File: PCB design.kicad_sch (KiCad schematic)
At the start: 19 parts

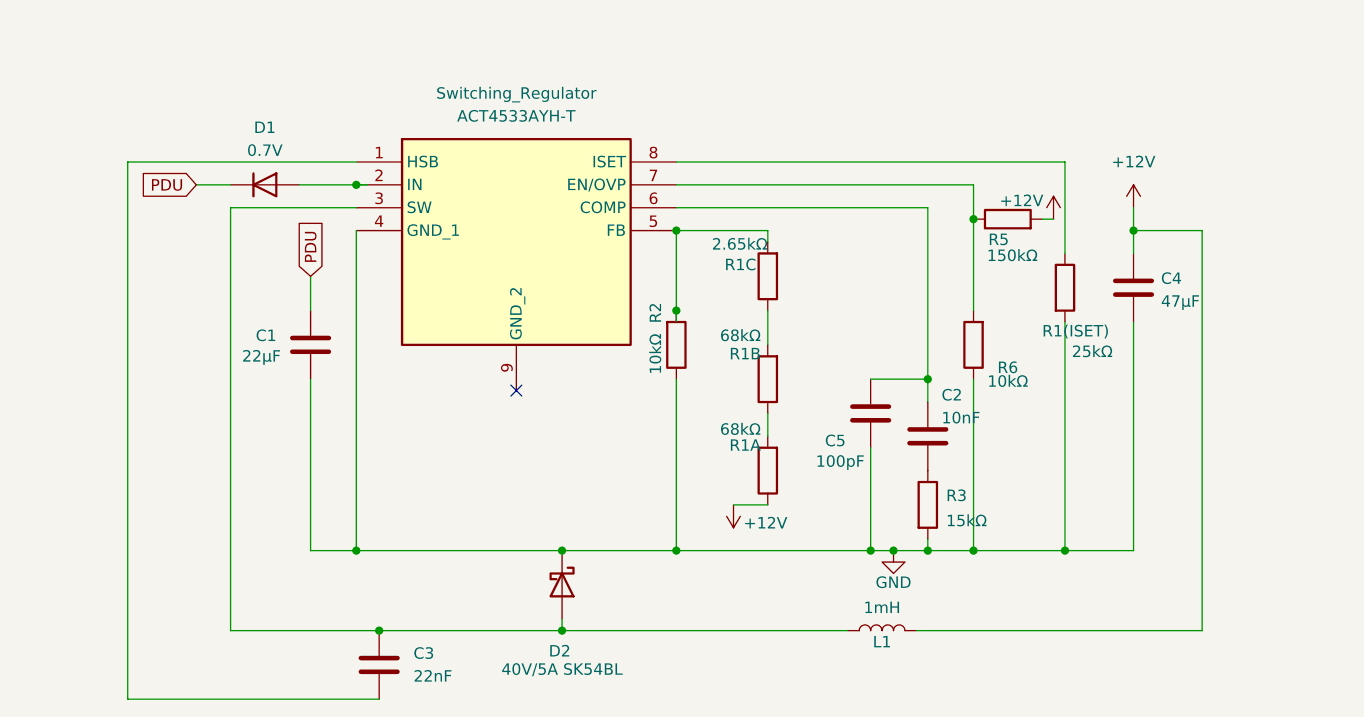
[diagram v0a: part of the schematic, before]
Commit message: added footprints to the components we have to buy.
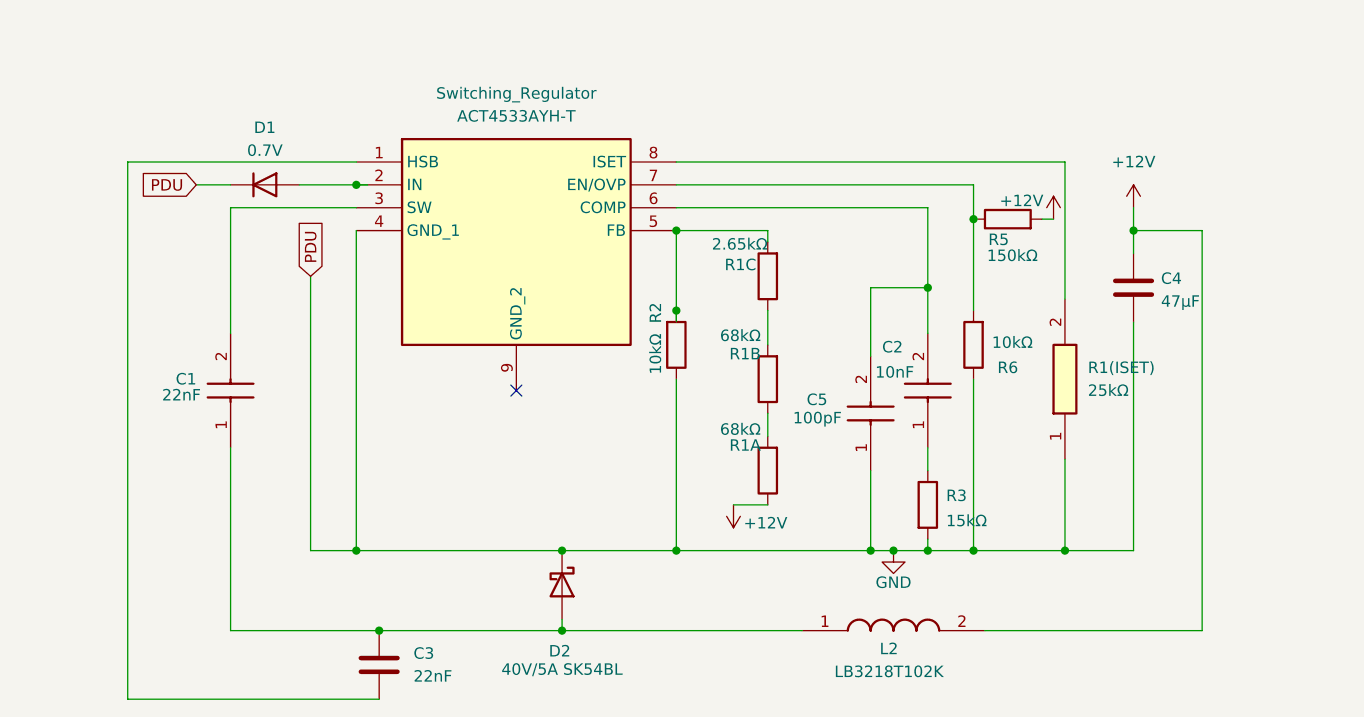
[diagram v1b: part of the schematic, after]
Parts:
- removed C1: 22µF, symbol Device:C
- removed C2: 10nF, symbol Device:C
- removed C5: 100pF, symbol Device:C
- removed L1: 1mH, symbol Device:L
- removed R1(ISET): 25kΩ, symbol Device:R
- added C1: 22nF, CAPPA3500W66L1100D600, symbol MKP1839110631:MKP1839110631
- added C2: 10nF, D103K69Y5PL63L0R, symbol D103K69Y5PL63L0R:D103K69Y5PL63L0R
- added C5: 100pF, CAPPA3100W60L1100D500, symbol MKT1813322405G:MKT1813322405G
- added L2: LB3218T102K, INDC3218X200N, symbol LB3218T102K:LB3218T102K
- added R1(ISET): 25kΩ, RESAD1526W69L610D229, symbol RN55E2502BRE6:RN55E2502BRE6
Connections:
- net PDU is gone; now on net GND: D1.1 (K), Male_Connector.2
- net +12V: now also L2.2
- net GND: now also C5.1 (+), R1(ISET).1
- net at C3.1, D2.2 (A): now also C1.1 (+), L2.1; no longer Switching_Regulator.3 (SW)
- net at Switching_Regulator.6 (COMP): now also C2.2, C5.2 (-)
- net at R3.1: now also C2.1
- net at Switching_Regulator.8 (ISET): now also R1(ISET).2
- new net: C1.2 (-), Switching_Regulator.3 (SW)

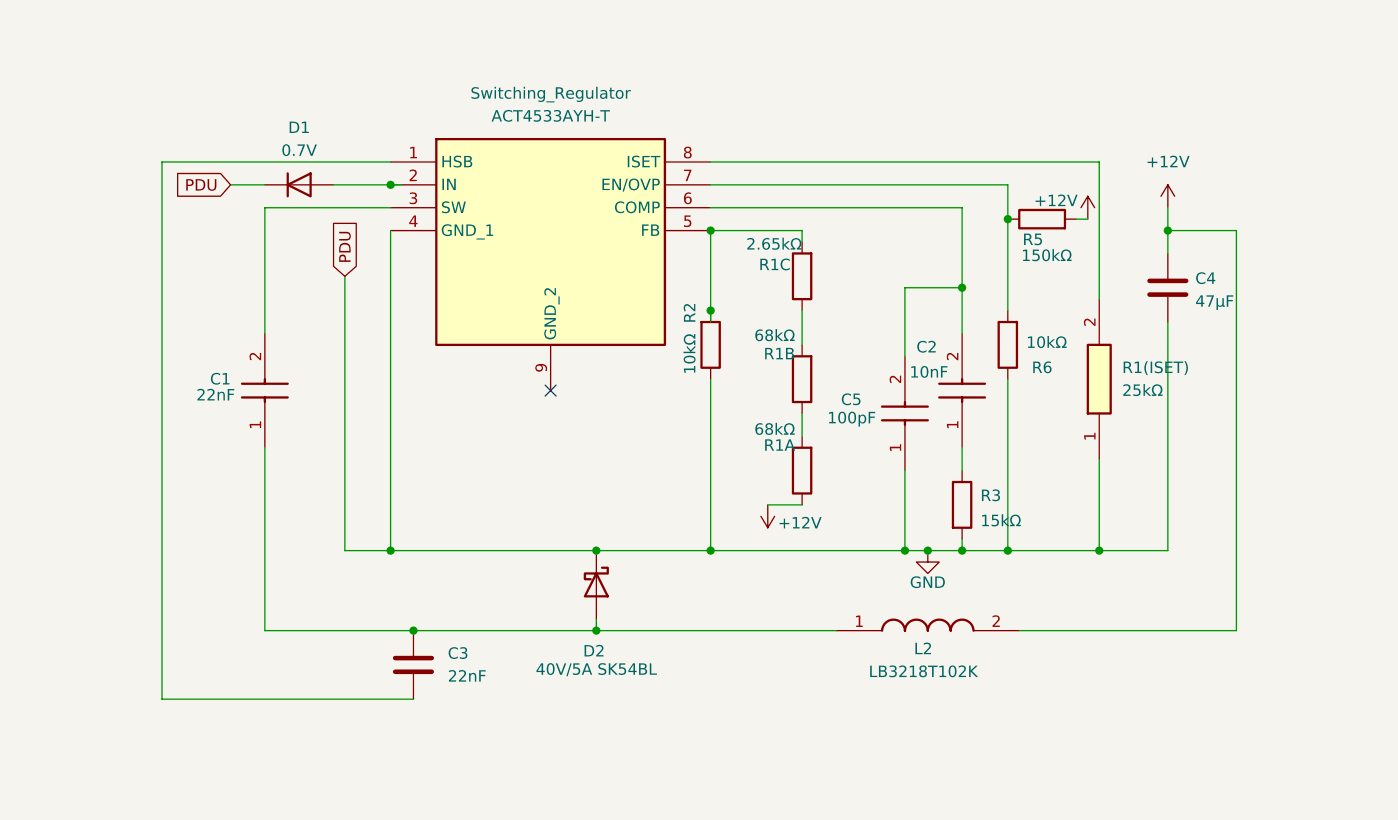
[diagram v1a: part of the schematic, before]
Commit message: added schotsky diode.
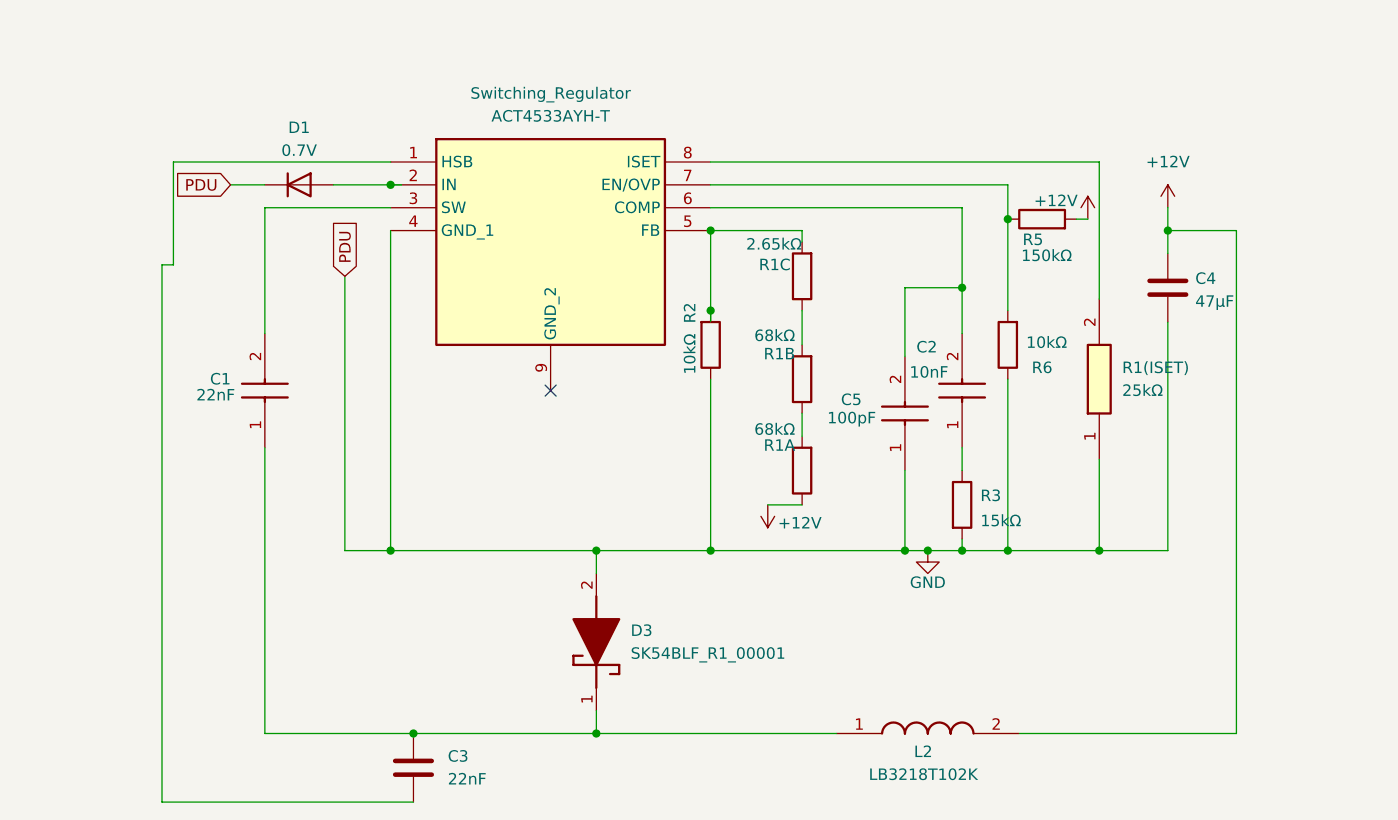
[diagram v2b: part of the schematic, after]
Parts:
- removed D2: 40V/5A SK54BL, Diode_SMD:D_0603_1608Metric, symbol Device:D_Schottky
- added D3: SK54BLF_R1_00001, SODFL5336X110N, symbol SK54BLF_R1_00001:SK54BLF_R1_00001
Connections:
- net GND: now also D3.2 (A)
- net at C1.1 (+), C3.1, L2.1: now also D3.1 (K)
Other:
- moved on the sheet: C3, L2

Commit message: Added a SMD footprint to all components, excluding the connectors
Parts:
- 150k1: renamed from 150kΩ; footprint (none) -> Resistor_SMD:R_01005_0402Metric_Pad0.57x0.30mm_HandSolder
- C1: footprint CAPPA3500W66L1100D600 -> Capacitor_SMD:C_01005_0402Metric_Pad0.57x0.30mm_HandSolder
- C2: footprint D103K69Y5PL63L0R -> Capacitor_SMD:C_01005_0402Metric_Pad0.57x0.30mm_HandSolder
- C3: footprint (none) -> Capacitor_SMD:C_1206_3216Metric_Pad1.33x1.80mm_HandSolder
- C4: footprint (none) -> Capacitor_SMD:C_1808_4520Metric_Pad1.72x2.30mm_HandSolder
- C5: footprint CAPPA3100W60L1100D500 -> Capacitor_SMD:C_1808_4520Metric_Pad1.72x2.30mm_HandSolder
- D1: footprint (none) -> Diode_SMD:D_2010_5025Metric_Pad1.52x2.65mm_HandSolder
- D3: footprint SODFL5336X110N -> Diode_SMD:D_2010_5025Metric_Pad1.52x2.65mm_HandSolder
- Female_Connector1: renamed from Female_Connector; footprint SFM-105-YY-XXX-D-A-K-TR -> Footprints:RESAD1526W69L610D229
- L2: footprint INDC3218X200N -> Inductor_SMD:L_10.4x10.4_H4.8
- Male_Connector1: renamed from Male_Connector; footprint TFM-105-02-XXX-D-WT -> Footprints:TFM-105-02-XXX-D-WT
- R1(ISET)1: renamed from R1(ISET); footprint RESAD1526W69L610D229 -> Resistor_SMD:R_01005_0402Metric_Pad0.57x0.30mm_HandSolder
- R1A1: renamed from R1A; footprint (none) -> Resistor_SMD:R_01005_0402Metric_Pad0.57x0.30mm_HandSolder
- R1B1: renamed from R1B; footprint (none) -> Resistor_SMD:R_01005_0402Metric_Pad0.57x0.30mm_HandSolder
- R1C1: renamed from R1C; footprint (none) -> Resistor_SMD:R_01005_0402Metric_Pad0.57x0.30mm_HandSolder
- R2, R3, R6: footprint (none) -> Resistor_SMD:R_01005_0402Metric_Pad0.57x0.30mm_HandSolder
- Switching_Regulator1: renamed from Switching_Regulator; footprint SOIC127P600X170-9N -> Footprints:SOIC127P600X170-9N
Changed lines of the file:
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@@
 	(wire
 		(pts
-			(xy 92.71 81.28) (xy 92.71 69.85)
+			(xy 91.44 69.85) (xy 91.44 140.97)
 		)
 		(stroke
@@
 	(wire
 		(pts
-			(xy 92.71 69.85) (xy 116.84 69.85)
+			(xy 91.44 69.85) (xy 116.84 69.85)
 		)
 		(stroke
@@
 	(wire
 		(pts
-			(xy 91.44 140.97) (xy 91.44 81.28)
-		)
-		(stroke
-			(width 0)
-			(type default)
-		)
-	)
-	(wire
-		(pts
 			(xy 152.4 69.85) (xy 195.58 69.85)
 		)
@@
 	(wire
 		(pts
-			(xy 91.44 81.28) (xy 92.71 81.28)
-		)
-		(stroke
-			(width 0)
-			(type default)
-		)
-	)
-	(wire
-		(pts
 			(xy 102.87 133.35) (xy 119.38 133.35)
 		)
@@
 		(in_pos_files yes)
 		(dnp no)
-		(property "Reference" "150kΩ"
+		(property "Reference" "150k1"
 			(at 189.738 80.264 90)
 			(show_name no)
@@
 			)
 		)
-		(property "Footprint" ""
+		(property "Footprint" "Resistor_SMD:R_01005_0402Metric_Pad0.57x0.30mm_HandSolder"
 			(at 189.23 77.978 90)
 			(hide yes)
@@
 			(project "PCB design"
 				(path "/1ee13f0d-22f2-4352-9e68-759581f4b836"
-					(reference "150kΩ")
+					(reference "150k1")
 					(unit 1)
 				)
@@
 			)
 		)
-		(property "Footprint" "INDC3218X200N"
+		(property "Footprint" "Inductor_SMD:L_10.4x10.4_H4.8"
 			(at 182.88 229.54 0)
 			(hide yes)
@@
 		(dnp no)
 		(fields_autoplaced yes)
-		(property "Reference" "R1(ISET)"
+		(property "Reference" "R1(ISET)1"
 			(at 198.12 92.7099 90)
 			(show_name no)
@@
 			)
 		)
-		(property "Footprint" "RESAD1526W69L610D229"
+		(property "Footprint" "Resistor_SMD:R_01005_0402Metric_Pad0.57x0.30mm_HandSolder"
 			(at 291.77 88.9 0)
 			(hide yes)
@@
 			(project "PCB design"
 				(path "/1ee13f0d-22f2-4352-9e68-759581f4b836"
-					(reference "R1(ISET)")
+					(reference "R1(ISET)1")
 					(unit 1)
 				)
@@
 			)
 		)
-		(property "Footprint" "SODFL5336X110N"
+		(property "Footprint" "Diode_SMD:D_2010_5025Metric_Pad1.52x2.65mm_HandSolder"
 			(at 233.35 120.65 0)
 			(hide yes)
@@
 			)
 		)
-		(property "Footprint" "CAPPA3500W66L1100D600"
+		(property "Footprint" "Capacitor_SMD:C_01005_0402Metric_Pad0.57x0.30mm_HandSolder"
 			(at 199.06 92.71 0)
 			(hide yes)
@@
 			)
 		)
-		(property "Footprint" ""
+		(property "Footprint" "Resistor_SMD:R_01005_0402Metric_Pad0.57x0.30mm_HandSolder"
 			(at 187.198 90.17 90)
 			(hide yes)
@@
 		(in_pos_files yes)
 		(dnp no)
-		(property "Reference" "R1A"
+		(property "Reference" "R1A1"
 			(at 161.798 101.346 0)
 			(show_name no)
@@
 			)
 		)
-		(property "Footprint" ""
+		(property "Footprint" "Resistor_SMD:R_01005_0402Metric_Pad0.57x0.30mm_HandSolder"
 			(at 164.338 104.14 90)
 			(hide yes)
@@
 			(project "PCB design"
 				(path "/1ee13f0d-22f2-4352-9e68-759581f4b836"
-					(reference "R1A")
+					(reference "R1A1")
 					(unit 1)
 				)
@@
 		(dnp no)
 		(fields_autoplaced yes)
-		(property "Reference" "Female_Connector"
+		(property "Reference" "Female_Connector1"
 			(at 259.08 83.82 0)
 			(show_name no)
@@
 			)
 		)
-		(property "Footprint" "SFM-105-YY-XXX-D-A-K-TR"
+		(property "Footprint" "Footprints:RESAD1526W69L610D229"
 			(at 266.7 186.36 0)
 			(hide yes)
@@
 			(project "PCB design"
 				(path "/1ee13f0d-22f2-4352-9e68-759581f4b836"
-					(reference "Female_Connector")
+					(reference "Female_Connector1")
 					(unit 1)
 				)
@@
 		(in_pos_files yes)
 		(dnp no)
-		(property "Reference" "R1C"
+		(property "Reference" "R1C1"
 			(at 161.29 81.28 0)
 			(show_name no)
@@
 			)
 		)
-		(property "Footprint" ""
+		(property "Footprint" "Resistor_SMD:R_01005_0402Metric_Pad0.57x0.30mm_HandSolder"
 			(at 164.338 82.55 90)
 			(hide yes)
@@
 			(project "PCB design"
 				(path "/1ee13f0d-22f2-4352-9e68-759581f4b836"
-					(reference "R1C")
+					(reference "R1C1")
 					(unit 1)
 				)
@@
 		(in_pos_files yes)
 		(dnp no)
-		(property "Reference" "R1B"
+		(property "Reference" "R1B1"
 			(at 161.798 91.186 0)
 			(show_name no)
@@
 			)
 		)
-		(property "Footprint" ""
+		(property "Footprint" "Resistor_SMD:R_01005_0402Metric_Pad0.57x0.30mm_HandSolder"
 			(at 164.338 93.98 90)
 			(hide yes)
@@
 			(project "PCB design"
 				(path "/1ee13f0d-22f2-4352-9e68-759581f4b836"
-					(reference "R1B")
+					(reference "R1B1")
 					(unit 1)
 				)
@@
 			)
 		)
-		(property "Footprint" ""
+		(property "Footprint" "Resistor_SMD:R_01005_0402Metric_Pad0.57x0.30mm_HandSolder"
 			(at 178.562 107.95 90)
 			(hide yes)
@@
 			)
 		)
-		(property "Footprint" ""
+		(property "Footprint" "Diode_SMD:D_2010_5025Metric_Pad1.52x2.65mm_HandSolder"
 			(at 106.68 72.39 0)
 			(hide yes)
@@
 			)
 		)
-		(property "Footprint" ""
+		(property "Footprint" "Capacitor_SMD:C_1808_4520Metric_Pad1.72x2.30mm_HandSolder"
 			(at 204.1652 87.63 0)
 			(hide yes)
@@
 		(dnp no)
 		(fields_autoplaced yes)
-		(property "Reference" "Male_Connector"
+		(property "Reference" "Male_Connector1"
 			(at 40.64 85.09 0)
 			(show_name no)
@@
 			)
 		)
-		(property "Footprint" "TFM-105-02-XXX-D-WT"
+		(property "Footprint" "Footprints:TFM-105-02-XXX-D-WT"
 			(at 48.26 187.63 0)
 			(hide yes)
@@
 			(project "PCB design"
 				(path "/1ee13f0d-22f2-4352-9e68-759581f4b836"
-					(reference "Male_Connector")
+					(reference "Male_Connector1")
 					(unit 1)
 				)
@@
 			)
 		)
-		(property "Footprint" "CAPPA3100W60L1100D500"
+		(property "Footprint" "Capacitor_SMD:C_1808_4520Metric_Pad1.72x2.30mm_HandSolder"
 			(at 270.18 95.25 0)
 			(hide yes)
@@
 		(dnp no)
 		(fields_autoplaced yes)
-		(property "Reference" "Switching_Regulator"
+		(property "Reference" "Switching_Regulator1"
 			(at 134.62 62.23 0)
 			(show_name no)
@@
 			)
 		)
-		(property "Footprint" "SOIC127P600X170-9N"
+		(property "Footprint" "Footprints:SOIC127P600X170-9N"
 			(at 148.59 164.77 0)
 			(hide yes)
@@
 			(project "PCB design"
 				(path "/1ee13f0d-22f2-4352-9e68-759581f4b836"
-					(reference "Switching_Regulator")
+					(reference "Switching_Regulator1")
 					(unit 1)
 				)
@@
 			)
 		)
-		(property "Footprint" ""
+		(property "Footprint" "Capacitor_SMD:C_1206_3216Metric_Pad1.33x1.80mm_HandSolder"
 			(at 120.3452 140.97 0)
 			(hide yes)
@@
 			)
 		)
-		(property "Footprint" "D103K69Y5PL63L0R"
+		(property "Footprint" "Capacitor_SMD:C_01005_0402Metric_Pad0.57x0.30mm_HandSolder"
 			(at 276.53 92.71 0)
 			(hide yes)
@@
 			)
 		)
-		(property "Footprint" ""
+		(property "Footprint" "Resistor_SMD:R_01005_0402Metric_Pad0.57x0.30mm_HandSolder"
 			(at 150.622 90.17 90)
 			(hide yes)
